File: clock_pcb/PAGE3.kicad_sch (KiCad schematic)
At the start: 29 parts, among them J3 FFC 24, J4 SM02B, J5 OLED, SW4 TS-1187A-B-A-B, SW5 TS-1187A-B-A-B, U5 DS1307Z+, Y2 32.768kHz

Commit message: break
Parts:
- removed C23: 1u, Capacitor_SMD:C_0402_1005Metric, symbol Device:C_Small
- added C25: 1u, Capacitor_SMD:C_0402_1005Metric, symbol Device:C_Small
- added C30: 0.1u, Capacitor_SMD:C_0402_1005Metric, symbol Device:C_Small
- added J4: 5V, Connector_JST:JST_SH_SM02B-SRSS-TB_1x02-1MP_P1.00mm_Horizontal, symbol Connector_Generic:Conn_01x02
- added Q3: 2N7002, Package_TO_SOT_SMD:SOT-23, symbol Transistor_FET:2N7002
- added R24, R25, R27: 10k, Resistor_SMD:R_0402_1005Metric, symbol Device:R_Small_US
- added R28: 1k, Resistor_SMD:R_0402_1005Metric, symbol Device:R_Small_US
- J5: renamed from J4; value SM02B -> 5V
- J6: renamed from J5; footprint Display:OLED-128O064D -> ftp:OLED-128O064D_edit
- R22: value 0 -> 10k; lcsc C17168 -> C25744
- renumbered C20 to C19, C21 to C20, C22 to C21, C24 to C22, C25 to C23, C26 to C24, C27 to C26, C28 to C27, C29 to C28, C30 to C29, R21 to R20, R20 to R21, R24 to R26, R25 to R29
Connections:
- net ADC_3V3 is gone; now on net GPIO2: J3.8 (Pin_8)
- net TX is gone; now on net GPIO4: J3.10 (Pin_10)
- net +3V3: now also C25.1, Q3.1 (G), R24.1, R25.1, R28.2
- net +5V: now also R22.1; no longer J5.2 (Pin_2)
- net GND: now also J3.13 (Pin_13), J3.18 (Pin_18), J3.21 (Pin_21), J3.24 (Pin_24), J3.5 (Pin_5), C25.2, C30.2, R27.2; no longer J3.15 (Pin_15), J3.22 (Pin_22), J3.7 (Pin_7)
- net GPIO2: no longer J3.11 (Pin_11), R20.2
- net GPIO4: no longer J3.13 (Pin_13), J6.19 (Pin_19), J6.20 (Pin_20), U5.5 (SDA)
- net GPIO5: now also J3.11 (Pin_11); no longer J3.14 (Pin_14), J6.18 (Pin_18), U5.6 (SCL)
- net WS2812_DOUT: now also J3.6 (Pin_6); no longer J3.21 (Pin_21)
- net PPS: now reaches U5.7 (SQW/OUT)
- net PPS: now also J3.7 (Pin_7), R24.2; no longer R22.1
- net I2C_SCL: now reaches J3.23 (Pin_23)
- net I2C_SCL: now also J6.18 (Pin_18), U5.6 (SCL)
- net GPIO0 renamed GPIO3
- net GPIO16 renamed GPIO28_ADC2
- net OLED_RES renamed OLED_RST
- net RX renamed GPIO6
- net SPI_MISO renamed BUTTON_0
- net BUTTON_0: no longer J3.16 (Pin_16)
- net SPI_MOSI renamed BUTTON_1
- net BUTTON_1: no longer J3.17 (Pin_17)
- net SPI_SCLK: no longer names the net of R22.2
- net SPI_SCLK: now also R20.2, Q3.3 (D); no longer J3.18 (Pin_18)
- net SPI_SS renamed GPIO27_ADC1
- new net: J4.2 (Pin_2), R28.1
- new net GPIO10: J3.17 (Pin_17)
- new net GPIO26_ADC0_LDR: C30.1, J4.1 (Pin_1), R27.1
- new net GPIO7: J3.14 (Pin_14)
- new net GPIO8: J3.15 (Pin_15)
- new net GPIO9: J3.16 (Pin_16)
- new net I2C_SDA: J3.22 (Pin_22), J6.19 (Pin_19), J6.20 (Pin_20), U5.5 (SDA)
- new net PWR_OFF_SW_N: J5.2 (Pin_2)
- new net WS2812_RGB_LED: Q3.2 (S), R25.2
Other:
- note added: "*EX"
- note added: "Hirose_FFC 24: FFC SAME C36268 FFC OPP. C24318"
- note added: "JST SR/SZ/SH SERIES: CRIMP SSH-003T HOUSING-2 SHR-02V-S CABLE-2 455-3619-ND HOUSING-4 SHR-04V-S CABLE-4 455-3632-ND"
- note added: "LDR: 1528-2141-ND 200KΩ (dark) to 10KΩ (10 lux brightness) Dark 150mV - 400mV Typ - 1.6V Light"
- note added: "Photocell/LDR"
- note added: "SWITCH"
- note added: "logic lvl shifter"
- note removed: "CABLE 455-3619-ND"
- note removed: "FFC SAME C36268 FFC OPP. C24318"
- note removed: "PWR OUT"
- moved on the sheet: BT1, C19, C20, C21, C22, D5, J5, R18, R19, R20, R21, R23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

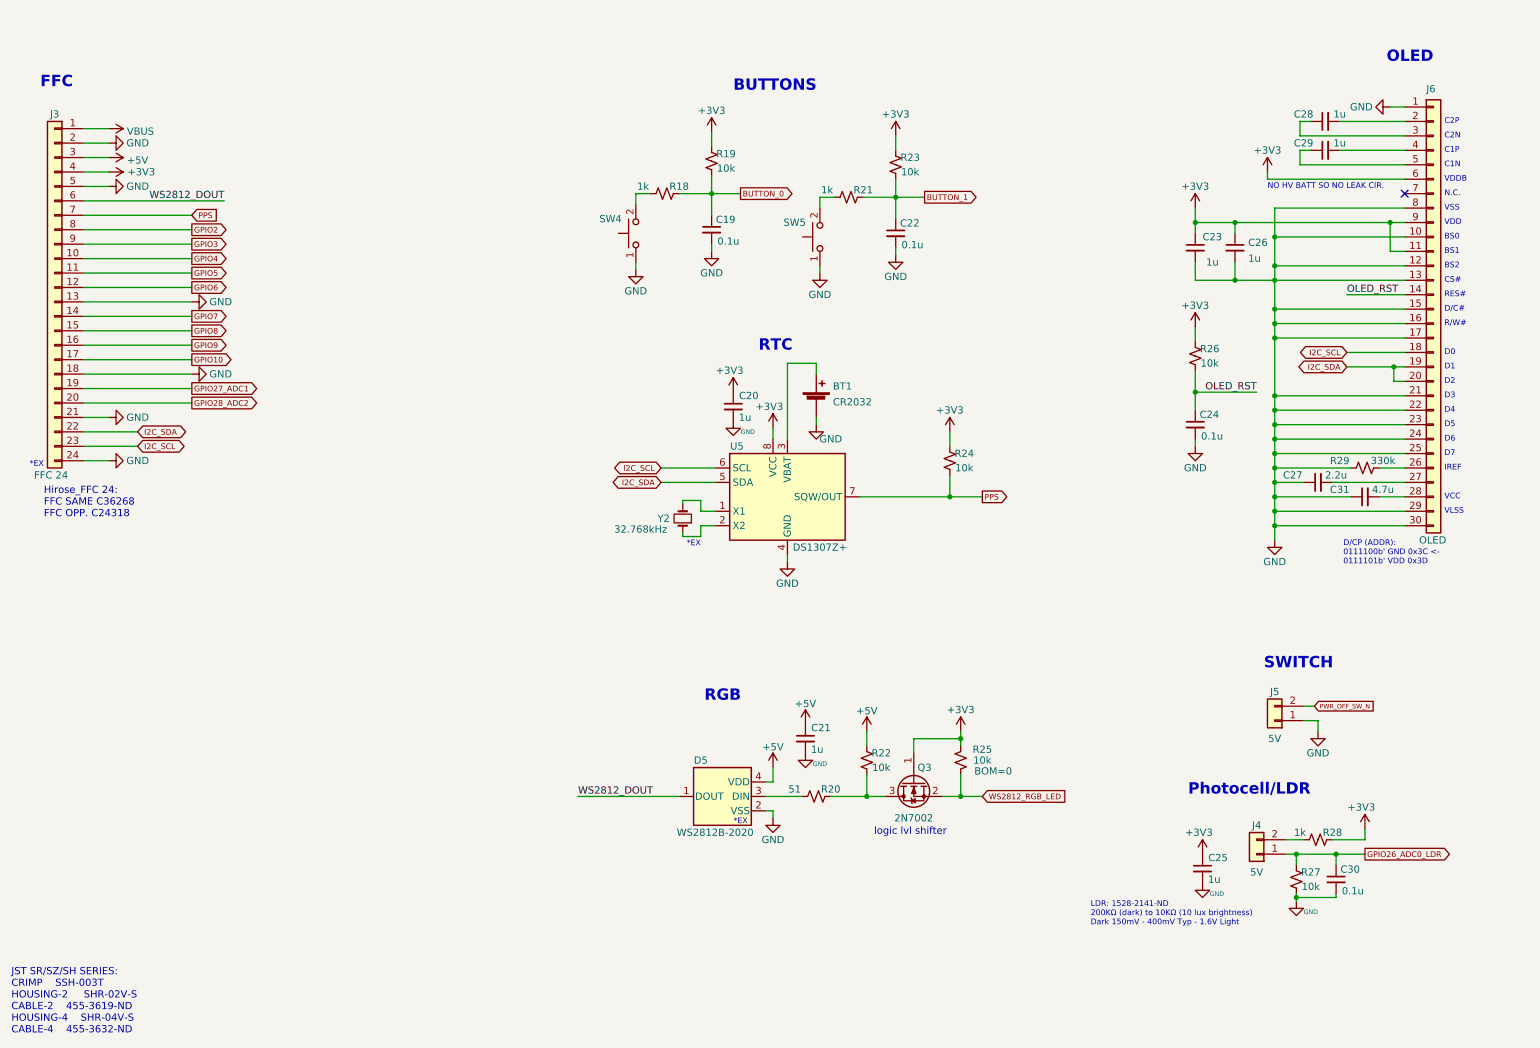
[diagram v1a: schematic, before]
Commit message: only brick nogging usbc left to add
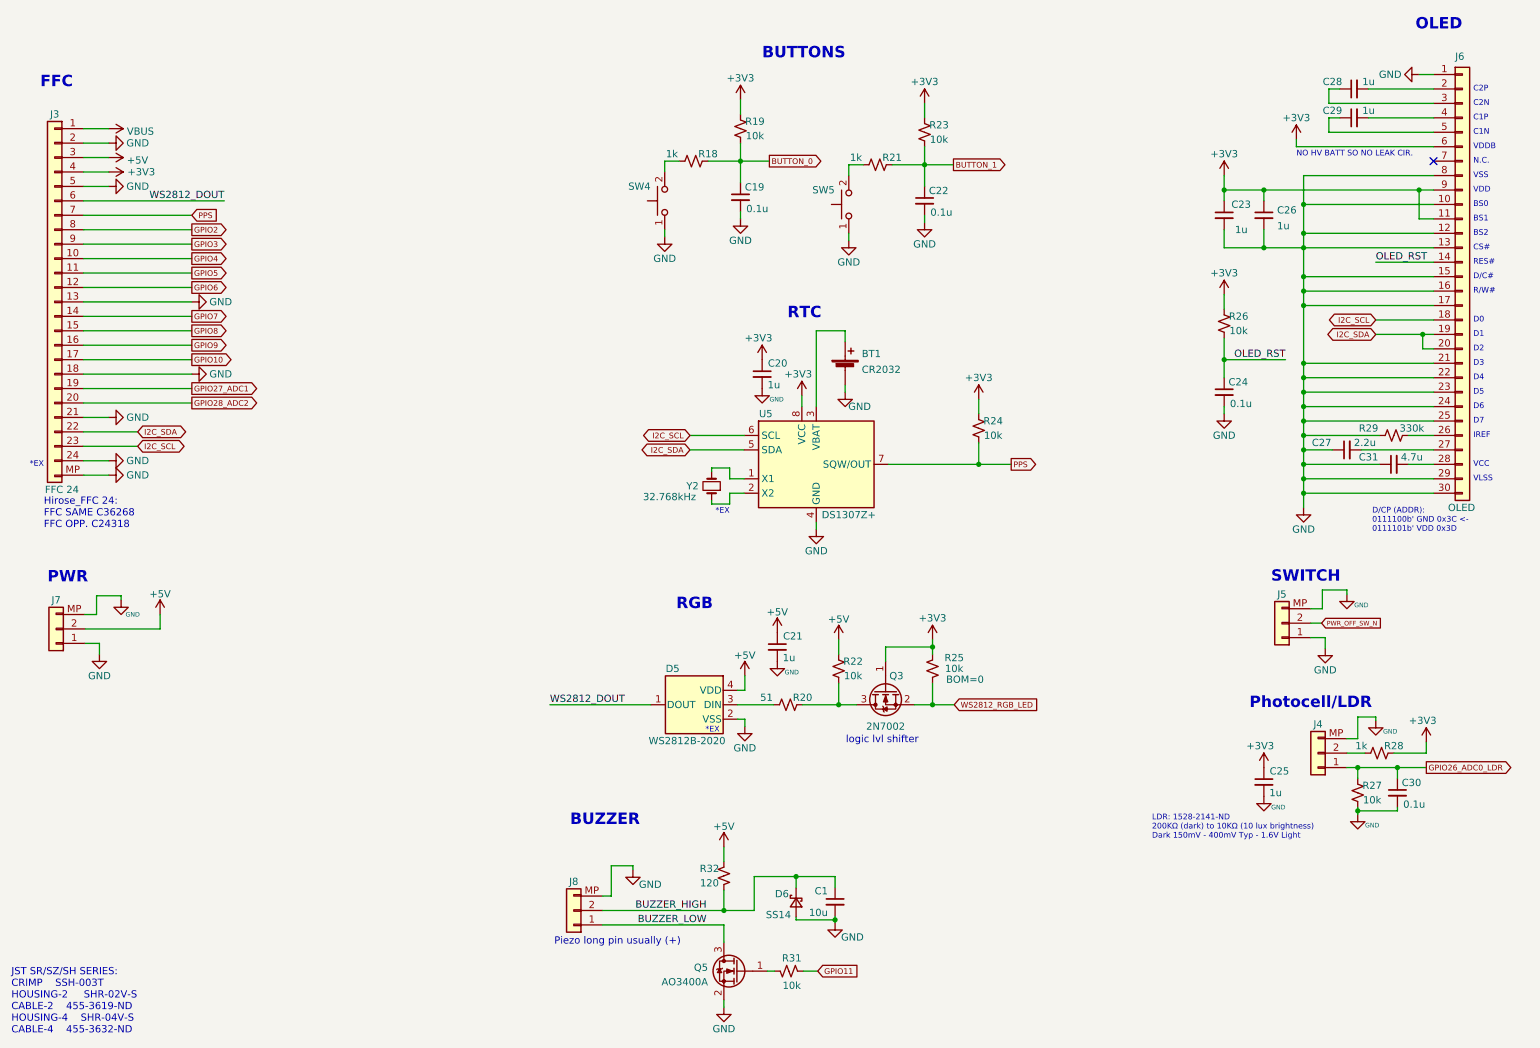
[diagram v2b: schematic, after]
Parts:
- added C1: 10u, Capacitor_SMD:C_0402_1005Metric, symbol Device:C_Small
- added D6: SS14, Diode_SMD:D_SMA, symbol Device:D_Schottky_Small
- added J7, J8: 5V, Connector_JST:JST_SH_SM02B-SRSS-TB_1x02-1MP_P1.00mm_Horizontal, symbol Connector_Generic:Conn_01x02
- added Q5: AO3400A, Package_TO_SOT_SMD:SOT-23, symbol Transistor_FET:AO3400A
- added R31: 10k, Resistor_SMD:R_0402_1005Metric, symbol Device:R_Small_US
- added R32: 120, Resistor_SMD:R_0402_1005Metric, symbol Device:R_Small_US
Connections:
- net +5V: now also J7.2 (Pin_2), R32.1
- net GND: now also J3.MP (MountingPoint), J4.MP (Mounting_Point), J5.MP (Mounting_Point), C1.2, D6.2 (A), J7.1 (Pin_1), J7.MP (Mounting_Point), J8.MP (Mounting_Point), Q5.2 (S)
- new net: Q5.1 (G), R31.2
- new net BUZZER_HIGH: C1.1, D6.1 (K), J8.2 (Pin_2), R32.2
- new net BUZZER_LOW: J8.1 (Pin_1), Q5.3 (D)
- new net GPIO11: R31.1
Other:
- note added: "BUZZER"
- note added: "PWR"
- note added: "Piezo long pin usually (+)"
- moved on the sheet: BT1, C19, C20, C21, C22, C23, C24, C25, C26, C27, C28, C29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
